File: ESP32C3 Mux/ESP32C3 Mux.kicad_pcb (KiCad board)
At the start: 2 copper layers, 13 parts, among them J1 6130XX243121_613020243121, J2 Conn_01x02_Socket, U1 ESP32C3, U2 TCA9548APWR, U8 STLQ015M33R

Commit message: finished layout
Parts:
- C7, C9: moved to B.Cu
- moved R3 30.7 mm to (174.6, 89.8), turned to 0 degrees
- moved R2 30.6 mm to (174.6, 87.3), turned to 0 degrees
- moved C1 22.0 mm to (170.3, 103.0)
- moved J1 21.7 mm to (159.1, 82.1), turned to 180 degrees
- moved C9 21.5 mm to (163.5, 124.1), turned to 180 degrees
- moved R1 15.3 mm to (174.6, 93.5), turned to 0 degrees
- moved C7 15.1 mm to (163.4, 126.6)
- moved U1 1.89 mm to (166.1, 114.6)
- moved U2 1.31 mm to (165.0, 99.2), turned to -90 degrees
- moved J2 1.27 mm to (149.8, 124.3)
- moved C10 0.71 mm to (166.8, 125.7)
- moved U8 0.70 mm to (163.5, 125.7)
- moved C8 0.65 mm to (160.1, 125.7)
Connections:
- J1 pad 8: /SDA3 -> /SCL2
- J1 pad 9: /SCL2 -> /SDA3
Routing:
- net +3V3: track 76.3 -> 102.7 mm, vias 0 -> 3
- net GND: track 24.2 -> 16.7 mm, vias 0 -> 10
- net /SCL2: track 13.6 -> 6.23 mm, vias 2 -> 0
- net /SDA: track 29.5 -> 23.3 mm
- net /SDA3: track 4.49 -> 9.55 mm
- net /SDA0: track 5.76 -> 10.0 mm
- net /SCL0: track 3.10 -> 6.89 mm
- net /SDA1: track 6.71 -> 9.86 mm
- net /SCL1: track 10.1 -> 7.15 mm, vias 2 -> 0
- net /SCL: track 33.8 -> 30.9 mm
- net /SCL4: track 13.8 -> 16.1 mm
- net /SDA4: track 11.7 -> 13.3 mm
- net /SCL3: track 8.23 -> 6.75 mm
- net /SDA2: track 7.94 -> 9.04 mm
- net unconnected-(U2-SC7-Pad20): track 0.74 -> 0.00 mm
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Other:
- board outline added: 30.9 x 44.7 mm

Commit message: drc errors
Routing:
- net +3V3: track 102.7 -> 101.1 mm
- net GND: track 16.7 -> 18.0 mm, vias 10 -> 11
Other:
- board size 30.9 x 44.7 mm -> 31.2 x 44.7 mm
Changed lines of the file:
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@@
 	(gr_rect
 		(start 145.7 84.1)
-		(end 176.6 128.8)
+		(end 176.9 128.8)
 		(stroke
 			(width 0.05)
@@
 	)
 	(segment
-		(start 173.99 92.1015)
-		(end 173.59 92.5015)
-		(width 0.381)
-		(layer "F.Cu")
-		(net 1)
-	)
-	(segment
 		(start 173.59 88.51)
 		(end 173.59 87.31)
@@
 		(start 166.8 124.7)
 		(end 166.8 123.9765)
-		(width 0.381)
-		(layer "F.Cu")
-		(net 1)
-	)
-	(segment
-		(start 173.59 92.5015)
-		(end 173.59 93.51)
 		(width 0.381)
 		(layer "F.Cu")
@@
 	)
 	(segment
+		(start 170.3 103.9)
+		(end 171.6 103.9)
+		(width 0.381)
+		(layer "F.Cu")
+		(net 2)
+	)
+	(segment
 		(start 160.1 126.6)
 		(end 158.6 126.6)
@@
 		(net 2)
 	)
+	(via
+		(at 171.6 103.9)
+		(size 0.6)
+		(drill 0.3)
+		(layers "F.Cu" "B.Cu")
+		(net 2)
+	)

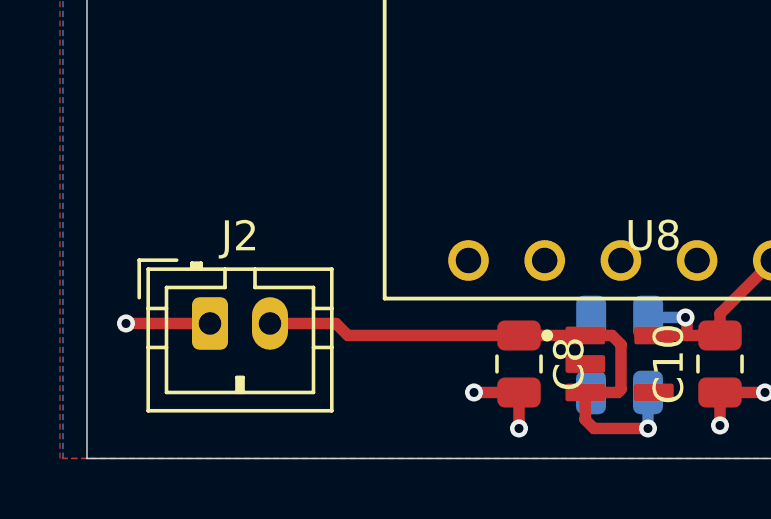
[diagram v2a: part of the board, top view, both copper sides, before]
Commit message: cleaned up some traces
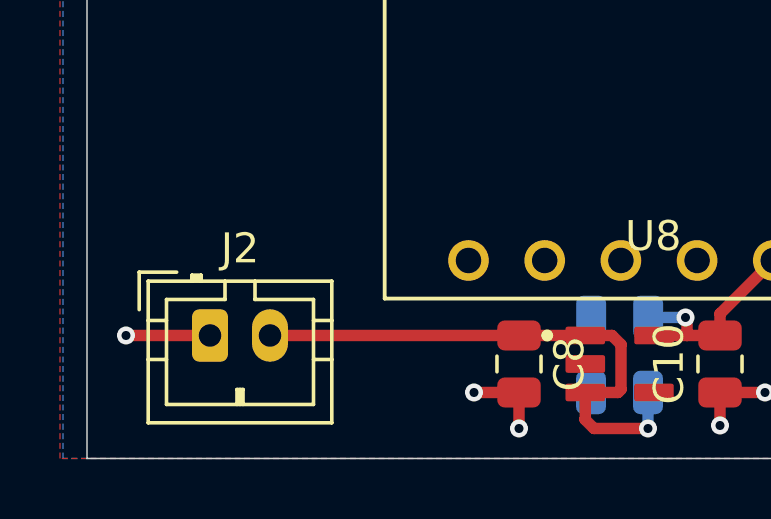
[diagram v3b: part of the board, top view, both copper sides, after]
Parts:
- moved J2 0.40 mm to (149.8, 124.7)
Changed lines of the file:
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@@
 	(footprint "Connector_JST:JST_PH_B2B-PH-K_1x02_P2.00mm_Vertical"
 		(layer "F.Cu")
-		(at 149.8 124.3)
+		(at 149.8 124.7)
 		(descr "JST PH series connector, B2B-PH-K (http://www.jst-mfg.com/product/pdf/eng/ePH.pdf), generated with kicad-footprint-generator")
 		(tags "connector JST PH vertical")
@@
 	)
 	(segment
-		(start 149.8 124.3)
-		(end 147 124.3)
+		(start 149.8 124.7)
+		(end 147 124.7)
 		(width 0.381)
 		(layer "F.Cu")
@@
 	)
 	(via
-		(at 147 124.3)
+		(at 147 124.7)
 		(size 0.6)
 		(drill 0.3)
@@
 	)
 	(segment
-		(start 160.1 124.7)
-		(end 154.4 124.7)
-		(width 0.381)
-		(layer "F.Cu")
-		(net 3)
-	)
-	(segment
 		(start 163.5 125)
 		(end 163.2 124.7)
@@
 	)
 	(segment
-		(start 154 124.3)
-		(end 151.8 124.3)
-		(width 0.381)
-		(layer "F.Cu")
-		(net 3)
-	)
-	(segment
 		(start 162.31 126.6)
 		(end 163.4 126.6)
@@
 	)
 	(segment
+		(start 160.1 124.7)
+		(end 151.8 124.7)
+		(width 0.381)
+		(layer "F.Cu")
+		(net 3)
+	)
+	(segment
 		(start 163.5 126.5)
 		(end 163.5 125)
@@
 		(width 0.381)
 		(layer "F.Cu")
-		(net 3)
-	)
-	(segment
-		(start 154.4 124.7)
-		(end 154 124.3)
-		(width 0.381)
-		(layer "F.Cu")

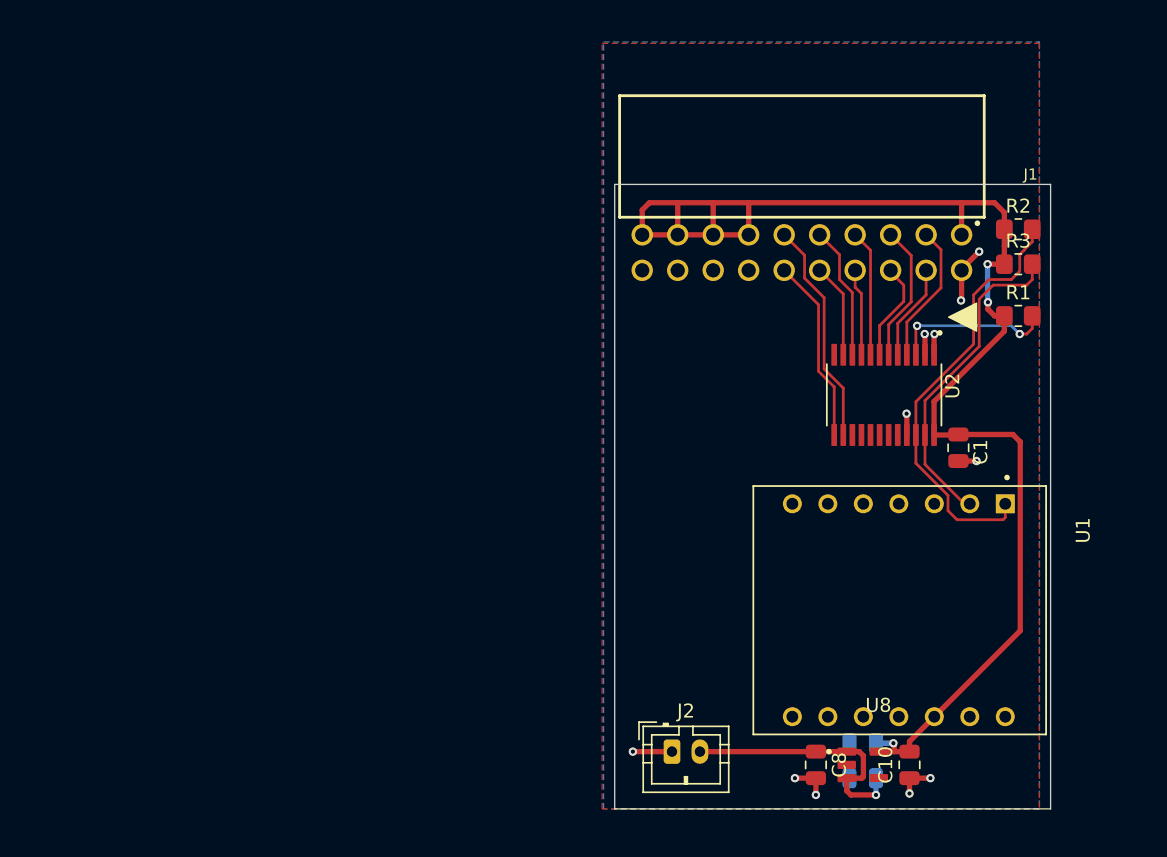
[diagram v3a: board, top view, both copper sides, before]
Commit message: removed mux and added 2 2x8 pin headers
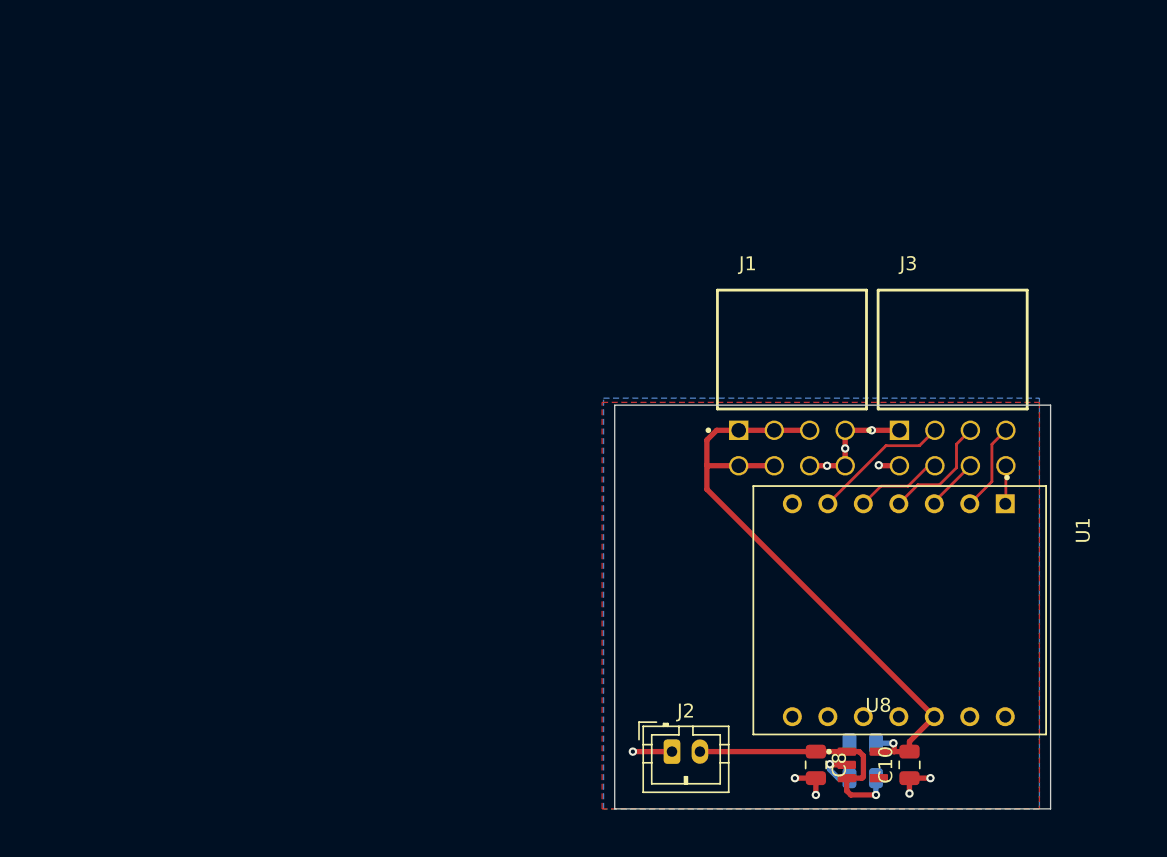
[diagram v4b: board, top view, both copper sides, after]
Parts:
- removed C1: 10uF, Capacitor_SMD:C_0805_2012Metric
- removed R1, R2, R3: 10k, Resistor_SMD:R_0805_2012Metric_Pad1.20x1.40mm_HandSolder
- removed U2: TCA9548APWR, ESP32C3 Mux:TCA9548APWR
- added J3: SSW-104-22-F-D-RA, ESP32C3 Mux:SAMTEC_SSW-104-22-F-D-RA, F.Cu at (166.1, 101.7)
- J1: value 6130XX243121_613020243121 -> SSW-104-22-F-D-RA; footprint ESP32C3 Mux:613020243121 -> ESP32C3 Mux:SAMTEC_SSW-104-22-F-D-RA
- moved J1 20.1 mm to (154.6, 101.7), turned to 0 degrees
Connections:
- U1 pad 2: /SDA -> /SDA1
- U1 pad 3: unconnected-(U1-D2-Pad3) -> /SDA2
- U1 pad 4: unconnected-(U1-D3-Pad4) -> /SDA3
- U1 pad 5: unconnected-(U1-D4-Pad5) -> /SDA4
- U1 pad 6: unconnected-(U1-D5-Pad6) -> /SDA5
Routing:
- net +3V3: track 101.1 -> 46.3 mm, vias 3 -> 1
- net /SCL: track 30.9 -> 2.74 mm
- net /SDA: track 23.3 -> 0.00 mm
- net /SCL4: track 16.1 -> 0.00 mm
- net Net-(U2-~{RESET}): track 11.7 -> 0.00 mm, vias 2 -> 0
- net /SDA0: track 10.0 -> 0.00 mm
- net /SDA5: track 0.00 -> 9.84 mm
- net /SCL1: track 7.15 -> 0.00 mm
- net /SDA4: track 13.3 -> 6.25 mm
- net /SCL0: track 6.89 -> 0.00 mm
- net /SCL3: track 6.75 -> 0.00 mm
- net /SCL2: track 6.23 -> 0.00 mm
- net /SDA2: track 9.04 -> 3.79 mm
- net GND: track 18.0 -> 21.8 mm, vias 11 -> 10
- net /SDA1: track 9.86 -> 6.72 mm
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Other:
- board size 31.2 x 44.7 mm -> 31.2 x 28.9 mm

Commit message: updates
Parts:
- removed J3: SSW-104-22-F-D-RA, ESP32C3 Mux:SAMTEC_SSW-104-22-F-D-RA
- C10, C7, C8, C9: footprint Capacitor_SMD:C_0805_2012Metric -> Capacitor_SMD:C_0805_2012Metric_Pad1.18x1.45mm_HandSolder
- J1: value SSW-104-22-F-D-RA -> 6130XX243121_613020243121; footprint ESP32C3 Mux:SAMTEC_SSW-104-22-F-D-RA -> ESP32C3 Mux:613020243121
- moved J1 9.78 mm to (162.3, 95.6), turned to 180 degrees
- moved J2 1.22 mm to (150.7, 125.6)
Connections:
- U1 pad 2: /SDA1 -> /SDA0
- U1 pad 3: /SDA2 -> /SDA1
- U1 pad 4: /SDA3 -> /SDA2
- U1 pad 5: /SDA4 -> /SDA3
- U1 pad 6: /SDA5 -> /SDA4
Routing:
- net /SCL: track 2.74 -> 18.6 mm
- net /SDA5: track 9.84 -> 0.00 mm
- net /SDA3: track 8.29 -> 3.19 mm
- net /SDA1: track 6.72 -> 3.19 mm
- net /SDA0: track 0.00 -> 3.19 mm
- net /SDA4: track 6.25 -> 3.19 mm
- net GND: track 21.8 -> 19.0 mm, vias 10 -> 13
- net /SDA2: track 3.79 -> 3.19 mm
- net +3V3: track 46.3 -> 45.8 mm
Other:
- board size 31.2 x 28.9 mm -> 29.1 x 31.4 mm

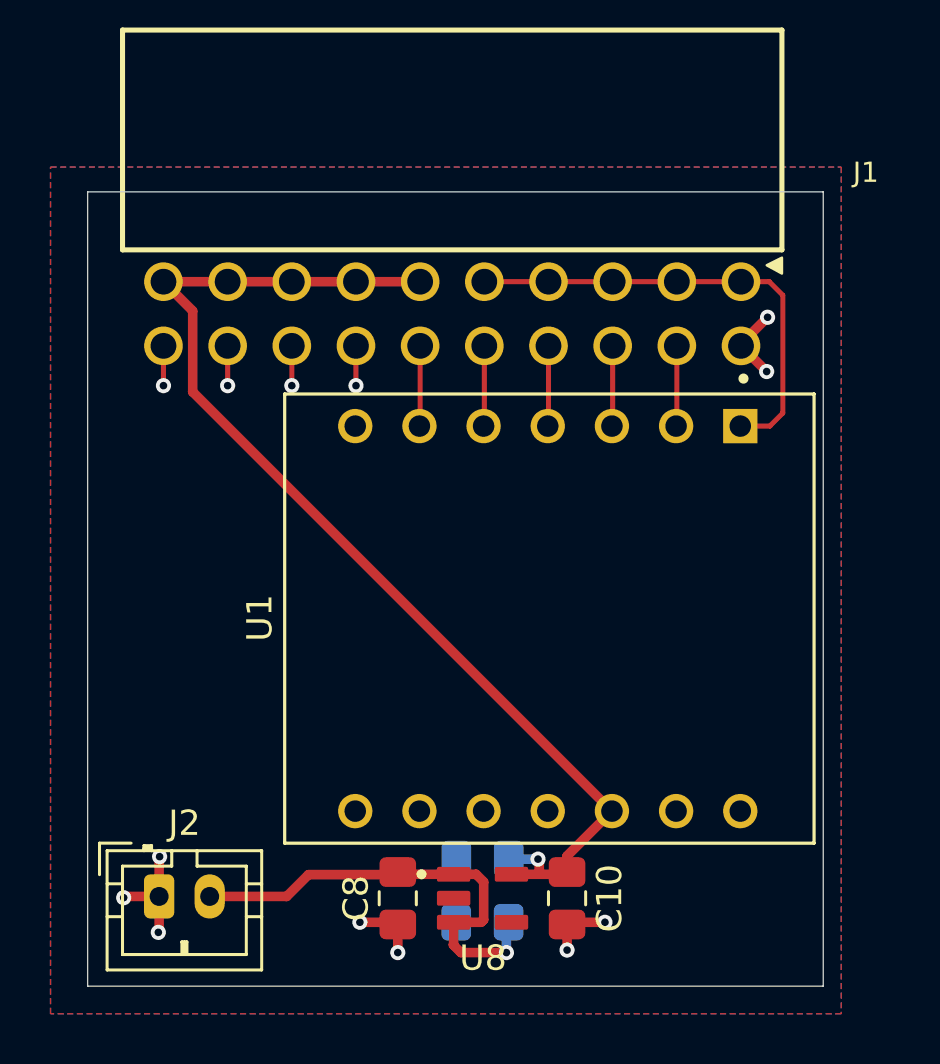
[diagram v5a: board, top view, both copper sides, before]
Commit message: Re-layout of sensor control board
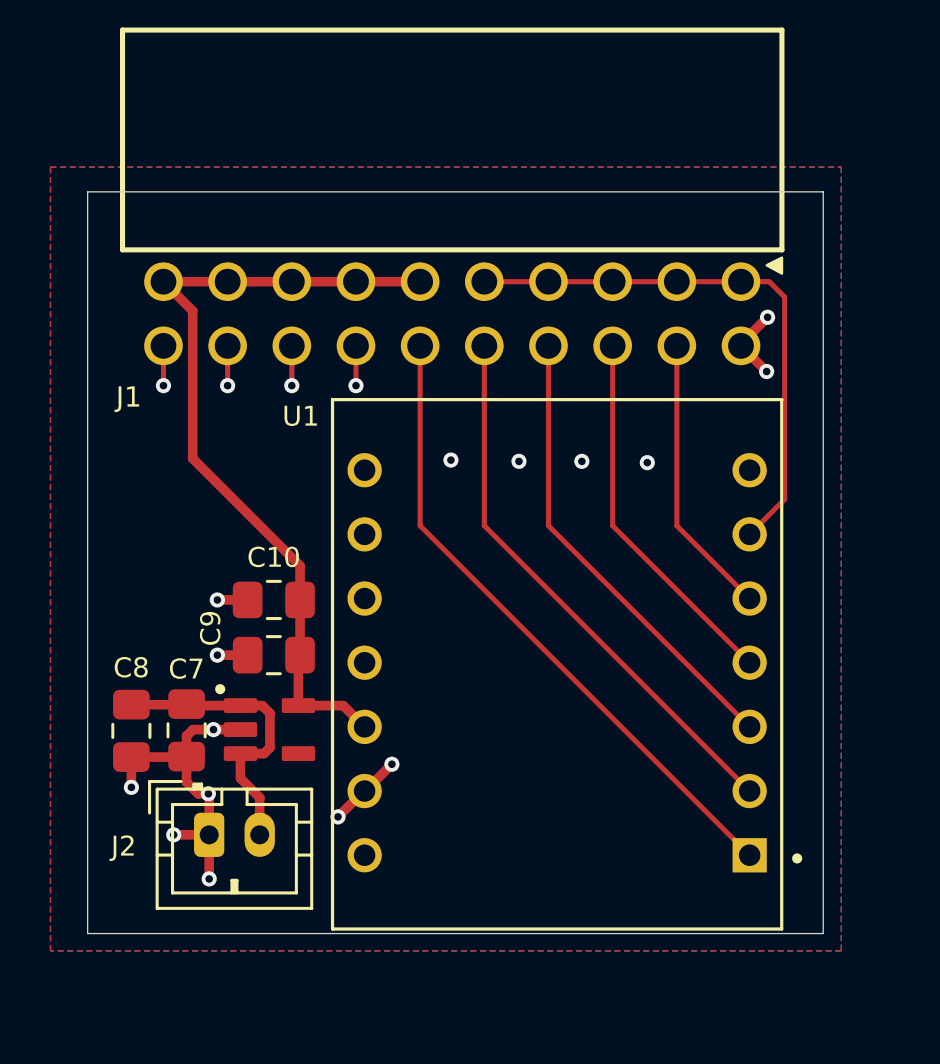
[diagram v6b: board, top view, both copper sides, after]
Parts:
- C7, C9: moved to F.Cu
- moved C10 16.6 mm to (155.2, 113.8), turned to 180 degrees
- moved C7 14.0 mm to (151.7, 119.0), turned to -90 degrees
- moved C8 12.5 mm to (149.6, 119.0)
- moved C9 11.6 mm to (155.2, 116.0)
- moved U8 10.8 mm to (155.0, 119.0)
- moved J2 3.14 mm to (152.6, 123.1)
- moved U1 1.84 mm to (166.4, 116.4), turned to 180 degrees
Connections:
- U1 pad 1: /SCL -> /SDA4
- U1 pad 2: /SDA0 -> /SDA3
- U1 pad 3: /SDA1 -> /SDA2
- U1 pad 4: /SDA2 -> /SDA1
- U1 pad 5: /SDA3 -> /SDA0
- U1 pad 6: /SDA4 -> /SCL
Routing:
- net /SDA4: track 3.19 -> 25.6 mm
- net /SDA3: track 3.19 -> 22.0 mm
- net /SDA2: track 3.19 -> 18.4 mm
- net +3V3: track 45.8 -> 32.2 mm, vias 1 -> 0
- net /SDA1: track 3.19 -> 14.8 mm
- net GND: track 19.0 -> 28.0 mm, vias 13 -> 19
- net /SDA0: track 3.19 -> 11.2 mm
- net +V_{BATT}: track 18.4 -> 11.8 mm, vias 1 -> 0
- net /SCL: track 18.6 -> 22.1 mm
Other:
- board size 29.1 x 31.4 mm -> 29.1 x 29.4 mm

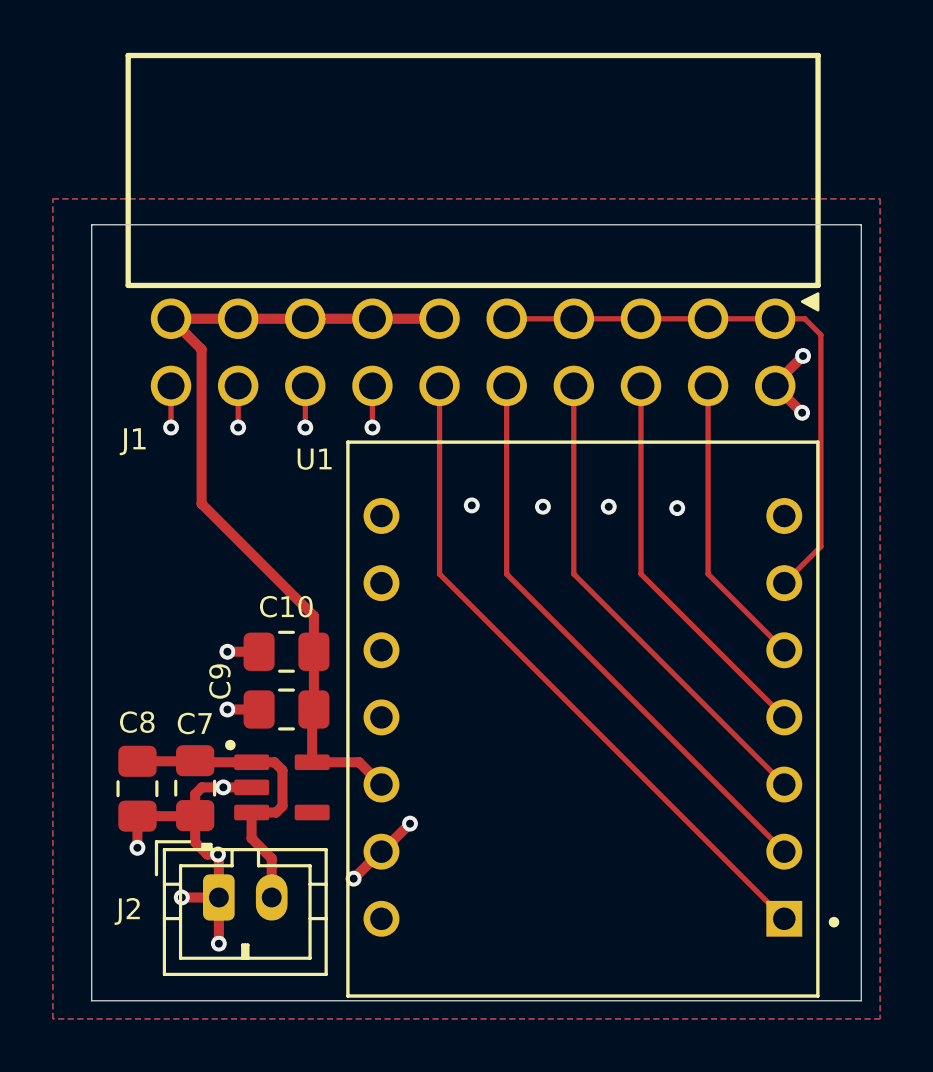
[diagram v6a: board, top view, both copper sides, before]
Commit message: Fixed battery issues, removed LDOs
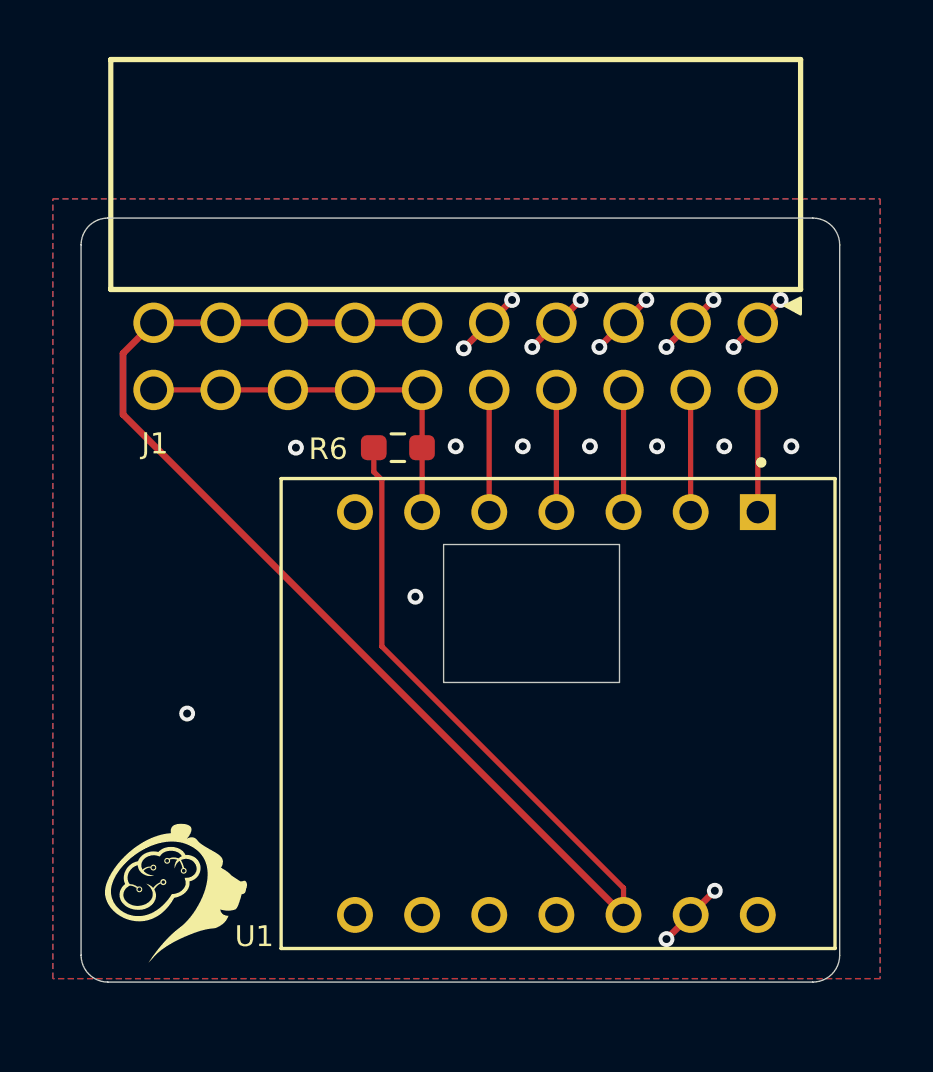
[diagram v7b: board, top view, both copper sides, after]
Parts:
- removed C10, C7: 10uF, Capacitor_SMD:C_0805_2012Metric_Pad1.18x1.45mm_HandSolder
- removed C8, C9: 1uF, Capacitor_SMD:C_0805_2012Metric_Pad1.18x1.45mm_HandSolder
- removed J2: Conn_01x02_Socket, Connector_JST:JST_PH_B2B-PH-K_1x02_P2.00mm_Vertical
- removed U8: STLQ015M33R, ESP32C3 Mux:SOT95P280X145-5N
- added G***: LOGO, Electric-Feel:ntablogo, F.Cu at (151.1, 122.9)
- added R6: 10k, Resistor_SMD:R_0603_1608Metric_Pad0.98x0.95mm_HandSolder, F.Cu at (159.4, 106.1)
- moved U1 0.96 mm to (165.5, 116.2), turned to -90 degrees
- moved J1 0.68 mm to (161.6, 95.8)
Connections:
- J1 pad 1: /SCL -> GND
- J1 pad 10: /SDA3 -> /SDA0
- J1 pad 12: /SDA4 -> /SCL
- J1 pad 14: GND -> /SCL
- J1 pad 16: GND -> /SCL
- J1 pad 18: GND -> /SCL
- J1 pad 2: GND -> /SDA4
- J1 pad 20: GND -> /SCL
- J1 pad 3: /SCL -> GND
- J1 pad 4: /SDA0 -> /SDA3
- J1 pad 5: /SCL -> GND
- J1 pad 6: /SDA1 -> /SDA2
- J1 pad 7: /SCL -> GND
- J1 pad 8: /SDA2 -> /SDA1
- J1 pad 9: /SCL -> GND
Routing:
- net +3V3: track 32.2 -> 62.5 mm
- net /SDA4: track 25.6 -> 4.62 mm
- net /SDA3: track 22.0 -> 4.62 mm
- net /SDA2: track 18.4 -> 4.62 mm
- net GND: track 28.0 -> 15.3 mm, vias 19 -> 21
- net +V_{BATT}: track 11.8 -> 0.00 mm
- net /SDA1: track 14.8 -> 4.62 mm
- net /SCL: track 22.1 -> 14.8 mm
- net /SDA0: track 11.2 -> 4.62 mm
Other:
- board size 29.1 x 29.4 mm -> 28.7 x 28.9 mm
